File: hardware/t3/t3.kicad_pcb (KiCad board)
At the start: 2 copper layers, 69 parts, among them P1 SMA, P2 CON, P3 UART1, P4 SWD, P5 USB_B, Q1 9012, SW1 SW_PUSH, SW2 SW_PUSH, U1 CC2591, U2 CC2400, U3 STM32F405RGTx, U4 LM1117-3.3, U5 LM1117-1.8, Y1 16MHz, Y2 32.768k, Y3 16MHz

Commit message: fix[5/x] ubertooth debug board
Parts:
- moved U4 99.3 mm to (97.8, 125.7)
- moved U5 99.3 mm to (110.5, 127.0)
- moved SW2 59.0 mm to (123.5, 129.3)
- moved U3 57.9 mm to (138.7, 107.9), turned to 270 degrees
- moved P5 51.6 mm to (162.5, 107.0)
- moved Y2 46.6 mm to (135.4, 95.5)
- moved C15 44.8 mm to (113.5, 113.8)
- moved C6 44.8 mm to (109.7, 113.8)
- moved U1 44.8 mm to (112.6, 108.8)
- moved C5 44.8 mm to (107.5, 109.2)
- moved C7 44.8 mm to (111.0, 113.8)
- moved L3 44.8 mm to (116.6, 105.7)
- moved R11 44.8 mm to (121.4, 101.6)
- moved R8 44.8 mm to (112.3, 113.8)
- moved R9 44.8 mm to (113.0, 104.4)
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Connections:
- C25 pad 1: GND -> +3V3
- C25 pad 2: Net-(C25-Pad2) -> GND
- C26 pad 2: Net-(C26-Pad2) -> +1V8
- C27 pad 1: GND -> +3V3
- C27 pad 2: Net-(C27-Pad2) -> GND
- C28 pad 2: Net-(C28-Pad2) -> +1V8
- C29 pad 2: Net-(C29-Pad2) -> /VBUS
- C30 pad 2: Net-(C30-Pad2) -> /VBUS
- U4 pad 2: /VBUS -> +3V3
- U4 pad 3: +3V3 -> /VBUS
- U4 pad 4: /VBUS -> +3V3
- U5 pad 2: /VBUS -> +1V8
- U5 pad 3: +1V8 -> /VBUS
- U5 pad 4: /VBUS -> +1V8
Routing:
- net /SO: track 0.00 -> 6.84 mm
- net /SI: track 0.00 -> 6.84 mm
- net /SCLK: track 0.00 -> 2.09 mm
- net /CSn: track 0.00 -> 1.63 mm
- net /DCLK: track 0.00 -> 1.59 mm
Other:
- board outline added: 105.2 x 68.6 mm
- net class Power added: clearance 0.2, trace_width 0.4, via_dia 0.6, via_drill 0.4
- rule trace_min: 0.2 -> 0.15
- rule via_min_size: 0.4 -> 0.6

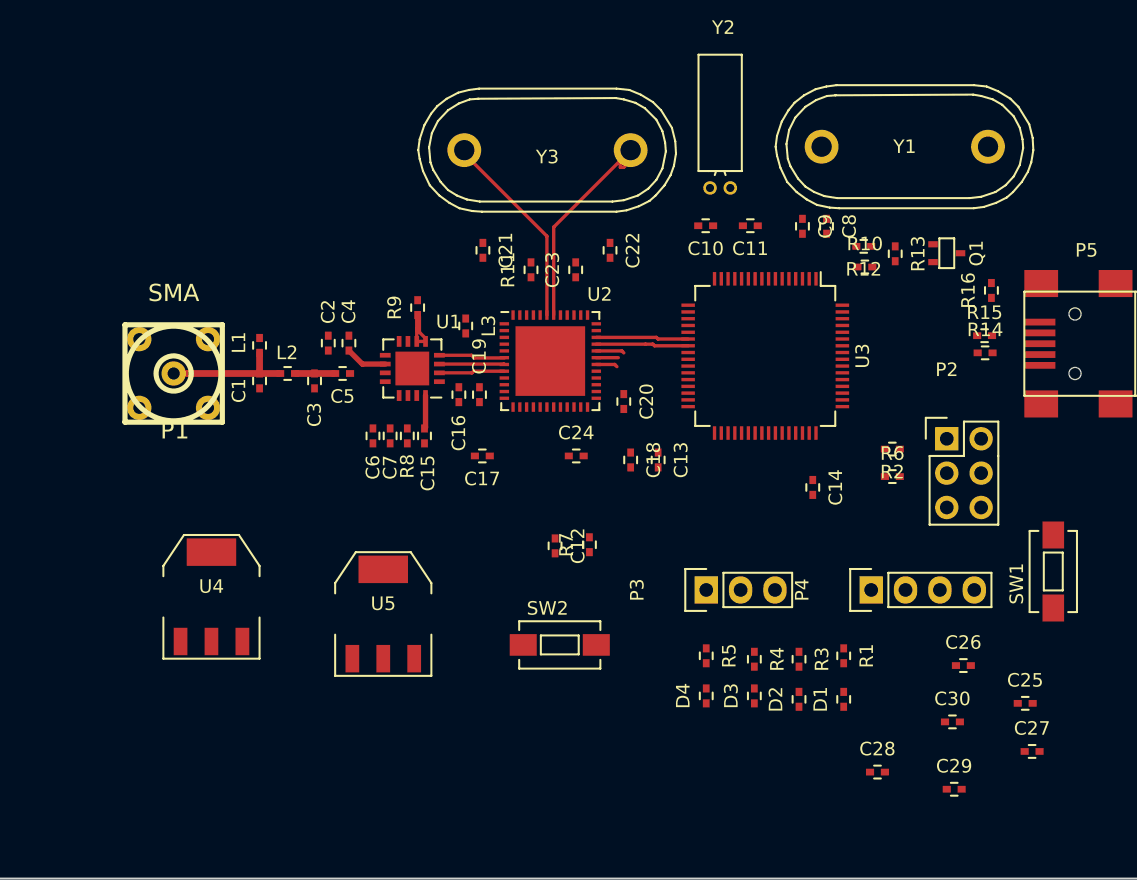
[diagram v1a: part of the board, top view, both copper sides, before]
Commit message: fix[6/x] ubertooth debug board
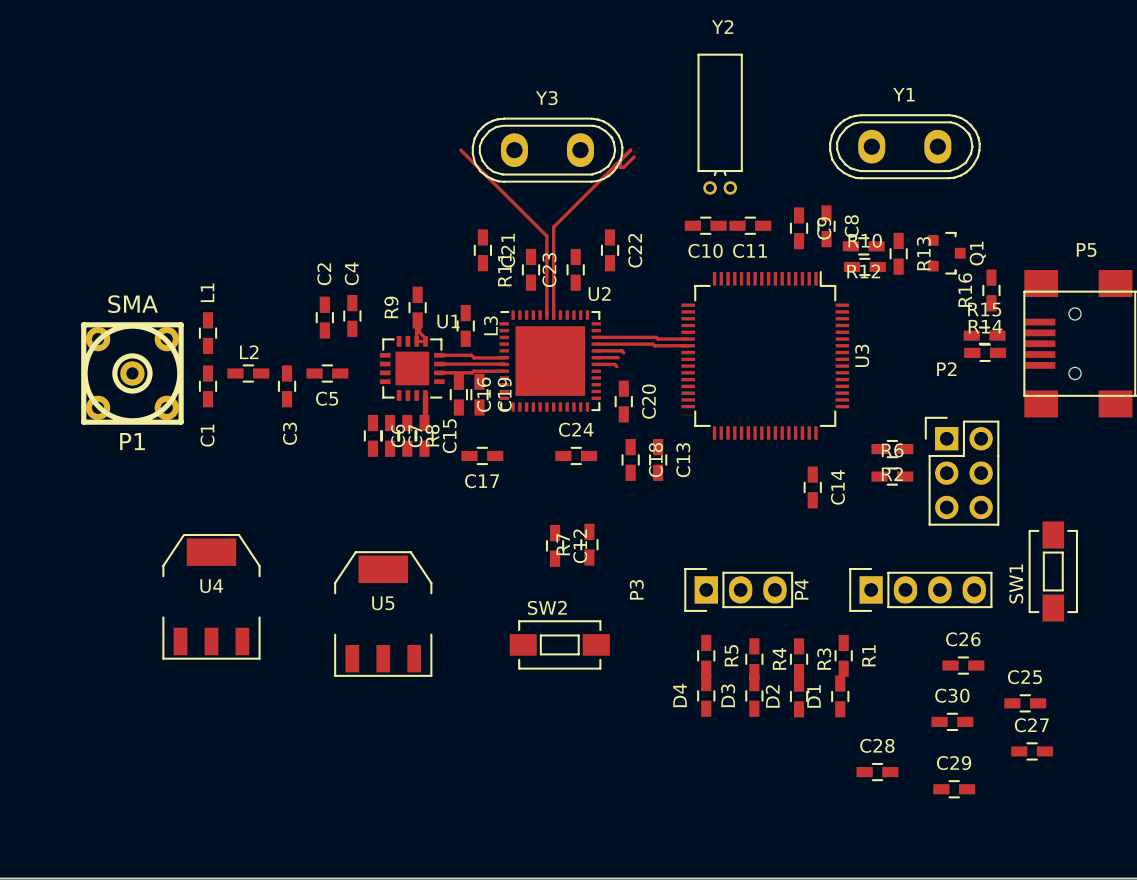
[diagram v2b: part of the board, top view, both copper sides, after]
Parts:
- C1, C10, C11, C12, C13, C14, C15, C16, C17, C18, C19, C2, C20, C21, C22, C23, C24, C25, C26, C27, C28, C29, C3, C30, C4, C5, C6, C7, C8, C9, D1, D2, D3, D4, L1, L2, L3, R1, R10, R11, R12, R13, R14, R15, R16, R2, R3, R4, R5, R6, R7, R8, R9: footprint Capacitors_SMD:C_0402 -> Capacitors_SMD:C_0603_HandSoldering
- Q1: footprint TO_SOT_Packages_SMD:SC-70 -> TO_SOT_Packages_SMD:SOT-23
- Y1, Y3: footprint Crystals:Crystal_HC48-U_Vertical -> Crystals:Crystal_HC50-U_Vertical
- moved L1 3.92 mm to (97.5, 106.2)
- moved C1 3.83 mm to (97.5, 110.2)
- moved P1 3.05 mm to (91.9, 109.2)
- moved L2 2.90 mm to (100.5, 109.2)
- moved C3 2.07 mm to (103.4, 110.2)
- moved C4 2.02 mm to (108.2, 105.0)
- moved C2 1.90 mm to (106.2, 105.1)
- moved C5 1.12 mm to (106.4, 109.2)
- moved D1 0.33 mm to (144.3, 133.1)
- moved C9 0.29 mm to (141.2, 98.5)
- moved R13 0.25 mm to (148.6, 100.4)
- moved D2 0.21 mm to (141.2, 133.1)
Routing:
- net Net-(C1-Pad2): track 9.40 -> 0.00 mm
- net +3V3: track 5.57 -> 2.47 mm
- net Net-(C3-Pad2): track 2.96 -> 0.00 mm

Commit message: update[7/x] ubertooth debug board
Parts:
- removed L3: NC, Capacitors_SMD:C_0603_HandSoldering
- added R17: 0R, Capacitors_SMD:C_0603_HandSoldering, F.Cu at (127.8, 112.5)
- added R18: 0R, Capacitors_SMD:C_0603_HandSoldering, F.Cu at (127.8, 114.0)
- C17, C4, C6: footprint Capacitors_SMD:C_0603_HandSoldering -> Capacitors_SMD:C_0805_HandSoldering
- moved R6 54.3 mm to (199.5, 134.6)
- moved R2 53.8 mm to (199.5, 130.8)
- moved P2 50.7 mm to (196.8, 137.9)
- moved U4 47.6 mm to (144.5, 134.6), turned to 90 degrees
- moved U5 34.0 mm to (144.5, 126.5), turned to 90 degrees
- moved P3 33.8 mm to (100.6, 126.5)
- moved SW1 32.8 mm to (191.8, 131.9), turned to 270 degrees
- moved P4 32.0 mm to (114.6, 126.5)
- moved C18 30.4 mm to (107.7, 93.7), turned to 90 degrees
- moved D1 29.2 mm to (149.9, 161.8)
- moved D2 29.2 mm to (146.8, 161.8)
- moved R3 29.2 mm to (146.8, 159.0)
- moved D3 29.2 mm to (143.5, 161.8)
- moved D4 29.2 mm to (140.0, 161.8)
- moved R1 29.2 mm to (150.1, 158.8)
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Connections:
- C16 pad 1: Net-(C16-Pad1) -> +3V3
- U1 pad 1: Net-(C16-Pad1) -> +3V3
- U2 pad 25: /GPIO3.3 -> Net-(R17-Pad1)
- U3 pad 10: Net-(U3-Pad10) -> /HGM
- U3 pad 11: Net-(U3-Pad11) -> /PAEN
- U3 pad 15: Net-(U3-Pad15) -> /ATEST1
- U3 pad 16: Net-(U3-Pad16) -> /ATEST2
- U3 pad 17: Net-(U3-Pad17) -> /GIO6
- U3 pad 29: Net-(U3-Pad29) -> /TX
- U3 pad 30: Net-(U3-Pad30) -> /RX
- U3 pad 33: Net-(U3-Pad33) -> /GPIO3.3
- U3 pad 34: Net-(U3-Pad34) -> /GIO1
- U3 pad 35: Net-(U3-Pad35) -> /GR
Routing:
- net /HGM: track 0.00 -> 32.4 mm, vias 0 -> 2
- net /PAEN: track 4.97 -> 34.6 mm, vias 0 -> 2
- net /ATEST2: track 0.00 -> 21.4 mm, vias 0 -> 2
- net /ATEST1: track 0.00 -> 19.4 mm, vias 0 -> 2
- net /DIO: track 0.00 -> 19.1 mm, vias 0 -> 2
- net /DCLK: track 1.59 -> 19.1 mm, vias 0 -> 2
- net /GR: track 0.00 -> 16.5 mm
- net /GIO1: track 0.00 -> 14.9 mm
- net Net-(R14-Pad1): track 0.00 -> 12.5 mm
- net Net-(R15-Pad1): track 0.00 -> 11.3 mm
- net Net-(C8-Pad1): track 0.00 -> 11.0 mm
- net Net-(C10-Pad1): track 0.00 -> 10.6 mm
- net Net-(C9-Pad1): track 0.00 -> 10.5 mm
- net Net-(C1-Pad2): track 0.00 -> 9.65 mm
- net Net-(R11-Pad1): track 0.00 -> 7.54 mm, vias 0 -> 2
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
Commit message: update
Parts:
- removed C30: 100nf, Capacitors_SMD:C_0603_HandSoldering
- added D5: LED, Capacitors_SMD:C_0603_HandSoldering, F.Cu at (177.8, 114.0)
- added L3: NC, Capacitors_SMD:C_0603_HandSoldering, F.Cu at (131.1, 84.3)
- added R19: 1K5, Capacitors_SMD:C_0603_HandSoldering, F.Cu at (175.8, 95.9)
- C13, C14, R6: moved to B.Cu
- C23: value 68pf -> 100nf; footprint Capacitors_SMD:C_0603_HandSoldering -> Capacitors_SMD:C_0805_HandSoldering
- C24, C28: value 100nf -> 10uf; footprint Capacitors_SMD:C_0603_HandSoldering -> Capacitors_SMD:C_0805_HandSoldering
- C25: footprint Capacitors_SMD:C_0603_HandSoldering -> Capacitors_SMD:C_0805_HandSoldering
- C26, C29: value 10uf -> 100nf
- R12: value 2k2 -> 0R(NC)
- R13: value 10k -> 0R
- R14: value 22R -> 330
- R15: value 22R -> 2k2
- R16: value 1K5 -> 10k
- R17, R18: value 0R -> 22R
- moved C12 67.6 mm to (154.5, 87.1)
- moved C24 65.8 mm to (173.2, 80.5), turned to 90 degrees
- moved U4 62.7 mm to (182.4, 84.6), turned to 0 degrees
- moved R7 61.7 mm to (154.5, 85.6), turned to 0 degrees
- moved C26 58.8 mm to (175.5, 81.0)
- moved R4 51.6 mm to (149.6, 107.8)
- moved R5 51.6 mm to (147.6, 107.8)
- moved R3 51.5 mm to (151.4, 107.8)
- moved R1 51.1 mm to (153.2, 107.8)
- moved D4 50.6 mm to (147.6, 111.7)
- moved D3 50.4 mm to (149.6, 111.7)
- moved D2 50.3 mm to (151.4, 111.7)
- moved D1 50.2 mm to (153.2, 111.7)
- moved P2 47.1 mm to (184.4, 92.5), turned to 270 degrees
- moved R18 47.1 mm to (173.7, 103.4), turned to 0 degrees
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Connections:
- C24 pad 1: +1V8 -> +3V3
- C25 pad 1: +3V3 -> GND
- C25 pad 2: GND -> +1V8
- C26 pad 1: GND -> +3V3
- C26 pad 2: +1V8 -> GND
- C27 pad 1: +3V3 -> GND
- C27 pad 2: GND -> +1V8
- C28 pad 2: +1V8 -> /VBUS
- R1 pad 1: Net-(R1-Pad1) -> /LED1
- R12 pad 1: Net-(Q1-Pad1) -> Net-(R12-Pad1)
- R12 pad 2: /USBEN -> +3V3
- R13 pad 1: Net-(Q1-Pad1) -> /GPIO3.3
- R13 pad 2: +3V3 -> Net-(R12-Pad1)
- R14 pad 1: Net-(R14-Pad1) -> /VBUS
- R14 pad 2: Net-(P5-Pad2) -> Net-(D5-Pad2)
- R15 pad 1: Net-(R15-Pad1) -> Net-(Q1-Pad1)
- R15 pad 2: Net-(P5-Pad3) -> /USBEN
- R16 pad 1: Net-(P5-Pad3) -> Net-(Q1-Pad1)
- R16 pad 2: Net-(Q1-Pad3) -> +3V3
- R17 pad 2: +3V3 -> Net-(P5-Pad2)
- R18 pad 1: /GPIO3.3 -> Net-(R18-Pad1)
- R18 pad 2: Net-(R17-Pad1) -> Net-(P5-Pad3)
- R3 pad 1: Net-(R3-Pad1) -> /LED2
- R4 pad 1: Net-(R4-Pad1) -> /LED3
- R5 pad 1: Net-(R5-Pad1) -> /LED4
- U2 pad 25: Net-(R17-Pad1) -> Net-(R12-Pad1)
- U3 pad 36: Net-(U3-Pad36) -> /LED4
- U3 pad 37: Net-(U3-Pad37) -> /LED3
- U3 pad 38: Net-(U3-Pad38) -> /LED2
- U3 pad 39: Net-(U3-Pad39) -> /LED1
- U3 pad 44: Net-(R14-Pad1) -> Net-(R17-Pad1)
- U3 pad 45: Net-(R15-Pad1) -> Net-(R18-Pad1)
- U3 pad 62: Net-(U3-Pad62) -> /USBEN
- U5 pad 3: /VBUS -> Net-(U5-Pad3)
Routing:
- net /UAER1_TX: track 0.00 -> 46.5 mm, vias 0 -> 1
- net /UAER1_RX: track 0.00 -> 44.8 mm, vias 0 -> 1
- net /NRST: track 0.00 -> 42.1 mm, vias 0 -> 2
- net Net-(P4-Pad3): track 0.00 -> 39.2 mm, vias 0 -> 1
- net Net-(P4-Pad2): track 0.00 -> 39.1 mm, vias 0 -> 1
- net /BOOT0: track 0.00 -> 29.4 mm, vias 0 -> 2
- net Net-(R18-Pad1): track 0.00 -> 20.8 mm
- net /BOOT1: track 0.00 -> 17.4 mm, vias 0 -> 1
- net Net-(R17-Pad1): track 4.94 -> 22.2 mm
- net Net-(R14-Pad1): track 12.5 -> 0.00 mm
- net Net-(P2-Pad4): track 0.00 -> 12.2 mm
- net /LED4: track 0.00 -> 11.7 mm
- net Net-(R15-Pad1): track 11.3 -> 0.00 mm
- net Net-(C11-Pad1): track 2.30 -> 13.1 mm
- net /LED3: track 0.00 -> 10.3 mm
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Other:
- board size 105.2 x 68.6 mm -> 81.3 x 45.7 mm

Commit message: update[8/x] add logo & fix layout
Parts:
- removed L3: NC, Capacitors_SMD:C_0603_HandSoldering
- added C30: 2.2pf, Capacitors_SMD:C_0603_HandSoldering, B.Cu at (128.6, 89.2)
- added G***: LOGO, Desktop:123, F.Cu at (114.8, 82.3)
- added L4: 1Kohms, Capacitors_SMD:C_0603_HandSoldering, B.Cu at (130.1, 84.7)
- added P6: power, Pin_Headers:Pin_Header_Straight_1x02, F.Cu at (181.9, 112.5)
- added P7: UART2, Pin_Headers:Pin_Header_Straight_1x03, F.Cu at (146.6, 117.1)
- added P8: Debug, Pin_Headers:Pin_Header_Straight_1x05, F.Cu at (171.7, 119.1)
- added t1: TST, t3:test_pin, B.Cu at (140.7, 86.9)
- added t2: TST, t3:test_pin, B.Cu at (140.0, 88.4)
- added t3: TST, t3:test_pin, B.Cu at (147.1, 101.9)
- added t4: TST, t3:test_pin, B.Cu at (148.6, 91.4)
- added t5: TST, t3:test_pin, B.Cu at (149.6, 98.0)
- added t6: TST, t3:test_pin, B.Cu at (153.7, 95.5)
- R6: moved to F.Cu
- Y1, Y3: footprint Crystals:Crystal_HC50-U_Vertical -> Crystals:Crystal_HC49-U_Vertical
- moved P4 4.83 mm to (128.8, 117.1)
- moved P3 4.06 mm to (118.9, 117.1)
- moved D5 2.09 mm to (175.8, 114.5)
- moved R14 2.09 mm to (177.5, 114.5)
- moved R15 2.04 mm to (169.2, 90.4)
- moved C19 1.02 mm to (137.7, 101.0)
- moved R6 1.02 mm to (171.6, 97.5)
- moved C25 0.51 mm to (159.9, 110.7)
- moved C29 0.51 mm to (173.5, 109.4)
- moved U5 0.51 mm to (166.9, 110.7)
- moved C13 0.36 mm to (156.9, 99.3)
- moved R8 0.25 mm to (132.1, 102.0)
- moved SW1 0.16 mm to (164.8, 117.3), turned to 0 degrees
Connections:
- C15 pad 1: +3V3 -> +3.3VADC
- C16 pad 1: +3V3 -> +3.3VADC
- C2 pad 2: +3V3 -> +3.3VADC
- C4 pad 2: +3V3 -> +3.3VADC
- C6 pad 1: +3V3 -> +3.3VADC
- C7 pad 1: +3V3 -> +3.3VADC
- P4 pad 1: +3V3 -> +3.3VADC
- SW1 pad 1: /BOOT0 -> +3.3VADC
- SW1 pad 2: +3V3 -> /BOOT0
- U1 pad 1: +3V3 -> +3.3VADC
- U1 pad 10: +3V3 -> +3.3VADC
- U1 pad 13: +3V3 -> +3.3VADC
- U1 pad 16: +3V3 -> +3.3VADC
- U3 pad 50: Net-(U3-Pad50) -> /debug4
- U3 pad 51: Net-(U3-Pad51) -> /UAER2_TX
- U3 pad 52: Net-(U3-Pad52) -> /UAER2_RX
- U3 pad 54: Net-(U3-Pad54) -> /debug5
- U3 pad 58: Net-(U3-Pad58) -> /debug1
- U3 pad 59: Net-(U3-Pad59) -> /debug2
- U3 pad 61: Net-(U3-Pad61) -> /debug3
- U5 pad 3: Net-(U5-Pad3) -> /VBUS
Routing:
- net GND: track 4.10 -> 537.7 mm, vias 0 -> 17
- net /VBUS: track 0.00 -> 176.7 mm, vias 0 -> 6
- net +3V3: track 2.76 -> 128.9 mm, vias 0 -> 7
- net +1V8: track 0.00 -> 109.0 mm, vias 0 -> 11
- net +3.3VADC: track 0.00 -> 106.7 mm, vias 0 -> 5
- net (no net): track 0.24 -> 41.2 mm, vias 0 -> 16
- net /UAER2_TX: track 0.00 -> 40.7 mm, vias 0 -> 1
- net /UAER2_RX: track 0.00 -> 39.7 mm, vias 0 -> 1
- net /debug3: track 0.00 -> 37.5 mm, vias 0 -> 1
- net /debug2: track 0.00 -> 35.3 mm, vias 0 -> 1
- net /debug1: track 0.00 -> 31.4 mm, vias 0 -> 1
- net /debug5: track 0.00 -> 29.0 mm, vias 0 -> 1
- net /debug4: track 0.00 -> 23.9 mm, vias 0 -> 1
- net Net-(P2-Pad3): track 0.00 -> 13.4 mm, vias 0 -> 1
- net Net-(P4-Pad3): track 39.2 -> 46.3 mm, vias 1 -> 2
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- added copper zone on B.Cu, net GND
- added copper zone on F.Cu, net GND
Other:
- board text added: "3.3v/DIO/CLK/GND"
- board text added: "Boot0"
- board text added: "GND/TX/RX"
- board text added: "Reset"
- board text added: "SWD"
- board text added: "TX/RX/GND"
- board text added: "Uart1"
- board text added: "Uart2"
- board text added: "VCC/GND"
